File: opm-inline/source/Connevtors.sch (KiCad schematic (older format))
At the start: 23 parts

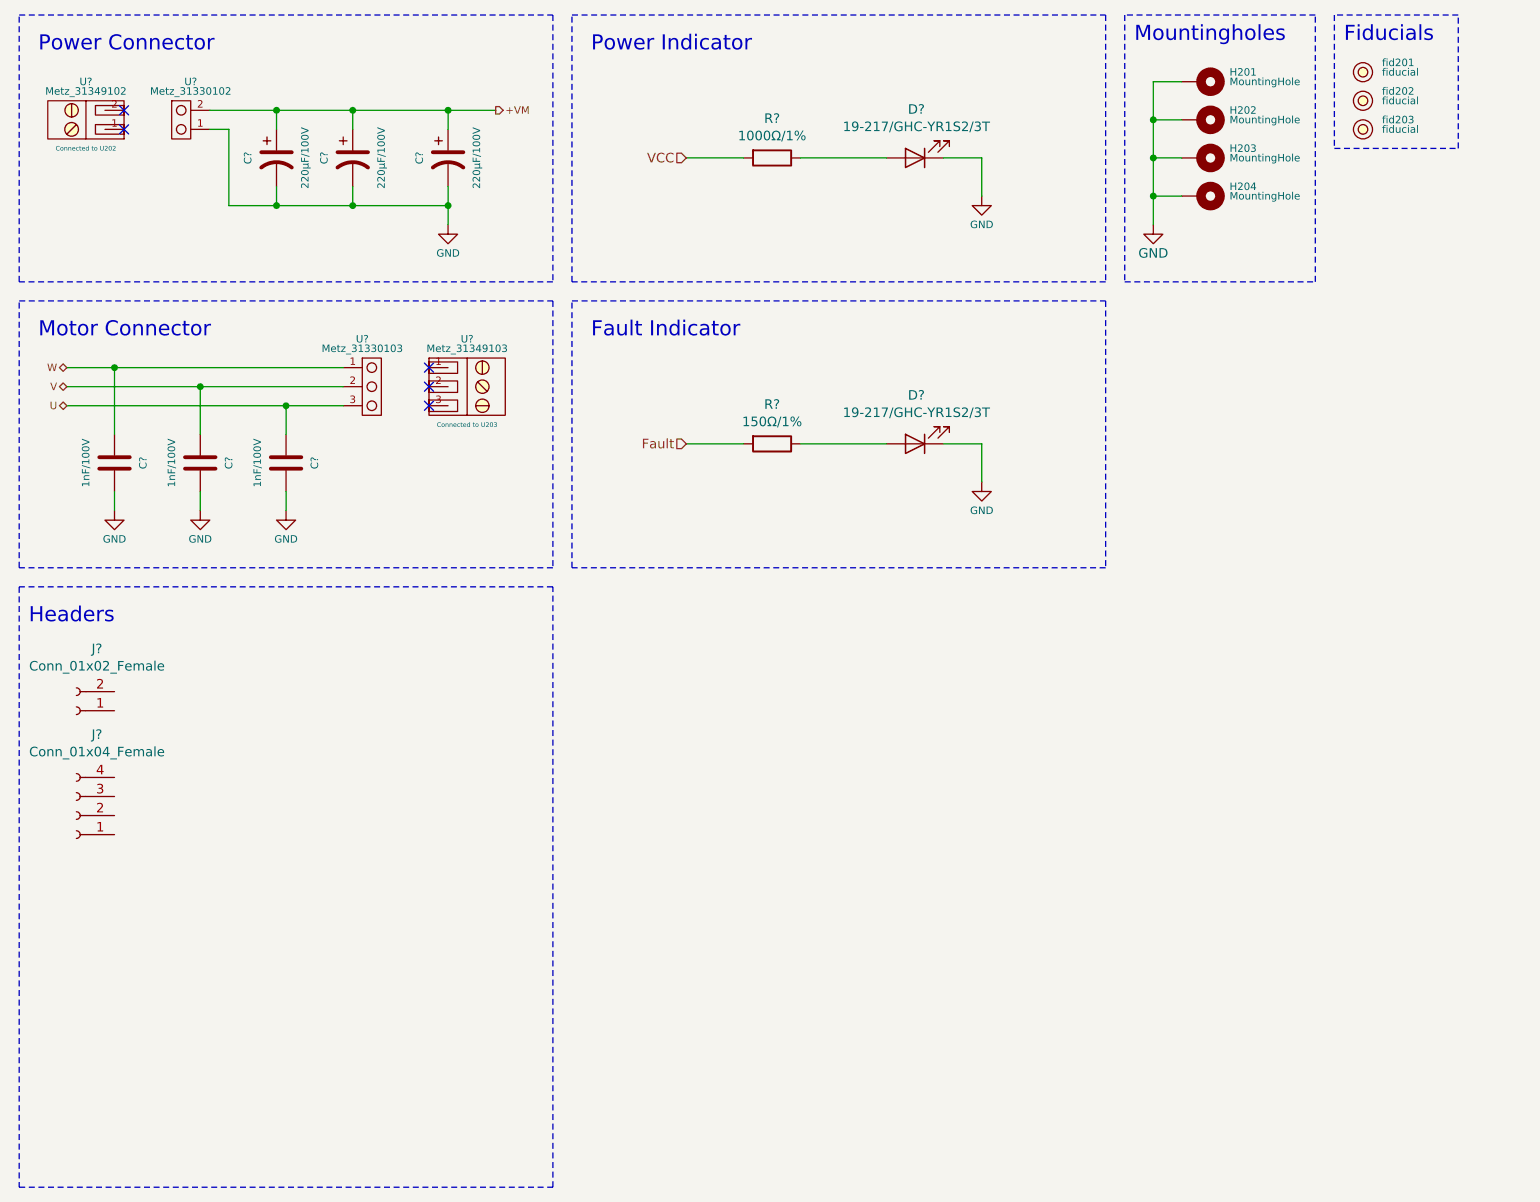
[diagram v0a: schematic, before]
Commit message: add headers
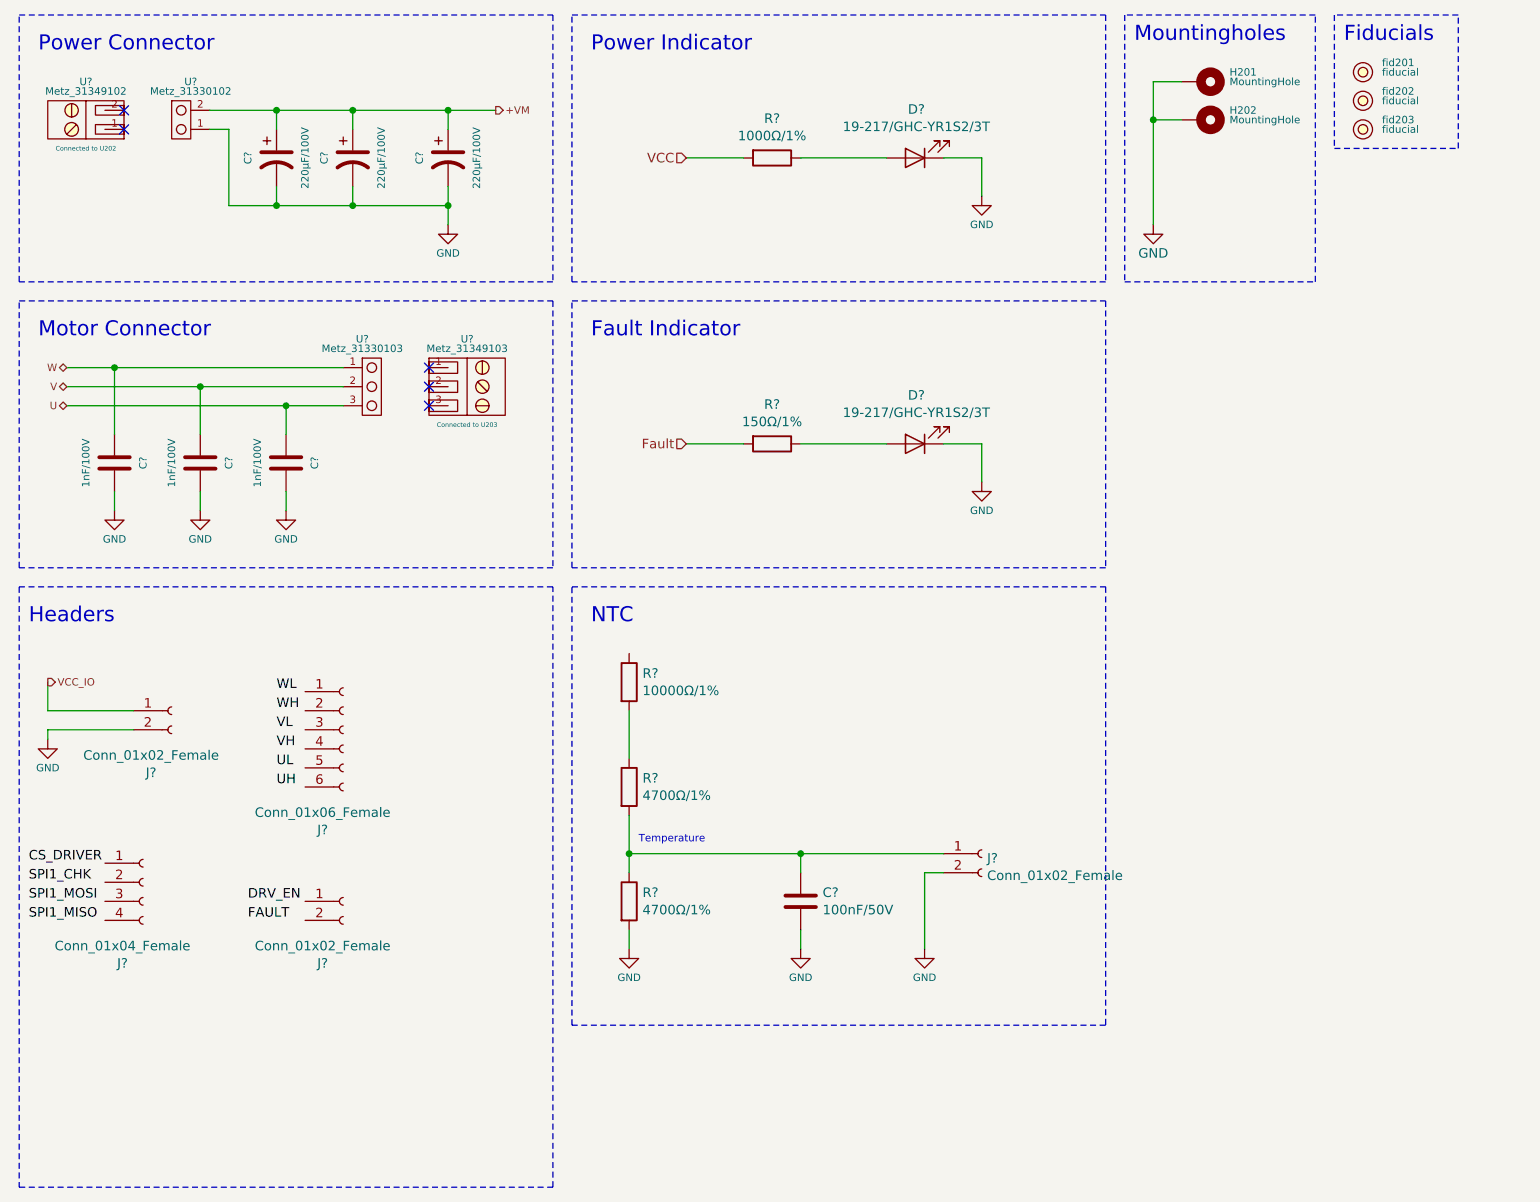
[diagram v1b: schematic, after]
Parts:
- removed H203, H204: MountingHole, MountingHole:MountingHole_3.2mm_M3_Pad, symbol opm-cache:Mechanical_MountingHole_Pad
- added C?: 100nF/50V, Capacitor_SMD:C_0603_1608Metric, symbol Device:C
- added J? (x2): Conn_01x02_Female, symbol Connector:Conn_01x02_Female
- added J?: Conn_01x06_Female, symbol Connector:Conn_01x06_Female
- added R? (x2): 4700Ω/1%, symbol Device:R
- added R?: 10000Ω/1%, Resistor_SMD:R_0603_1608Metric, symbol Device:R
- J? (x2): footprint (none) -> Connector_PinHeader_2.00mm:PinHeader_1x02_P2.00mm_Vertical
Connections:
- net GND: now also J?.2 (Pin_2), C?.2, J?.2 (Pin_2), R?.2
- net VCC_IO: now reaches J?.1 (Pin_1)
- new net: C?.1, J?.1 (Pin_1), R?.1, R?.2
- new net: R?.1, R?.2
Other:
- note added: "NTC"
- note added: "Temperature"
- moved on the sheet: J?

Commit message: prepare for pcb
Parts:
- R17, R18: renamed from R?; footprint (none) -> Resistor_SMD:R_0603_1608Metric
- fid201, fid202, fid203: footprint Fiducial:Fiducial_0.5mm_Dia_1mm_Outer -> Fiducial:Fiducial_0.5mm_Mask1mm
- gave numbers to parts that had none: 21
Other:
- moved on the sheet: J1, J2, J3, J4

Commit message: fix connections
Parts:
- added R21: 1000Ω/1%, symbol Device:R
- added R22: 0Ω, symbol Device:R
- added R23: 1500Ω/1%, symbol Device:R
- added R24: 4700Ω/1%, symbol Device:R
- C13, C15, C16: footprint Capacitor_THT:CP_Radial_D12.5mm_P5.00mm -> Libraries:CAPE830X690N
- J1: footprint Connector_PinHeader_2.00mm:PinHeader_1x02_P2.00mm_Vertical -> Connector_PinHeader_2.54mm:PinHeader_1x04_P2.54mm_Vertical
- J2: footprint Connector_PinHeader_2.00mm:PinHeader_1x02_P2.00mm_Vertical -> Connector_PinHeader_2.54mm:PinHeader_1x02_P2.54mm_Vertical
- J3: footprint (none) -> Connector_PinHeader_2.54mm:PinHeader_1x06_P2.54mm_Vertical
- J4, J5: footprint (none) -> Connector_PinHeader_2.54mm:PinHeader_1x02_P2.54mm_Vertical
- U1: footprint (none) -> TerminalBlock:TerminalBlock_bornier-2_P5.08mm
- U4: footprint (none) -> TerminalBlock:TerminalBlock_bornier-3_P5.08mm
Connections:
- net DRV_EN: now also J4.1 (Pin_1)
- net FAULT: now also J4.2 (Pin_2)
- net GND: now also R22.2, R24.2
- net SPI1_CHK: now also J1.2 (Pin_2)
- net SPI1_MISO: now also J1.3 (Pin_3), J1.4 (Pin_4)
- net UH: now also J3.6 (Pin_6)
- net UL: now also J3.5 (Pin_5)
- net VH: now also J3.4 (Pin_4)
- net VL: now also J3.3 (Pin_3)
- net WH: now also J3.2 (Pin_2)
- net WL: now also J3.1 (Pin_1)
- net ~CS_DRIVER: now reaches J1.1 (Pin_1)
- new net +VCC_IO: R21.1, R23.1
- new net SPE: R23.2, R24.1
- new net VOFS: R21.2, R22.1
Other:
- note added: "Not Mounted"
- note added: "VCC_IO SPE"
- note added: "VCC_IO VOFS"
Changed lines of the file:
@@
 F 0 "U4" V 2700 2700 39  0000 C CNN
 F 1 "Metz_31349103" V 2750 2700 39  0000 C CNN
-F 2 "" H 2925 2770 39  0001 C CNN
-F 3 "http://www.farnell.com/datasheets/2336351.pdf" H 2925 2770 39  0001 C CNN
+F 2 "TerminalBlock:TerminalBlock_bornier-3_P5.08mm" H 2925 2770 39  0001 C CNN
+F 3 "" H 2925 2770 39  0001 C CNN
 F 4 "Connected to U203" V 3150 2700 24  0000 C CNN "Info"
 	1    2950 2700
@@
 F 0 "U1" V 1150 1300 39  0000 C CNN
 F 1 "Metz_31349102" V 1100 1300 39  0000 C CNN
-F 2 "" H 950 1250 39  0001 C CNN
+F 2 "TerminalBlock:TerminalBlock_bornier-2_P5.08mm" H 950 1250 39  0001 C CNN
 F 3 "" H 950 1250 39  0001 C CNN
 F 4 "Connected to U202" V 800 1300 24  0000 C CNN "Info"
@@
 F 0 "C15" V 2200 1500 39  0000 C CNN
 F 1 "220μF/100V" V 2500 1500 39  0000 C CNN
-F 2 "Capacitor_THT:CP_Radial_D12.5mm_P5.00mm" V 2550 1500 39  0001 C CNN
+F 2 "Libraries:CAPE830X690N" V 2550 1500 39  0001 C CNN
 F 3 "~" H 2350 1500 39  0001 C CNN
 F 4 "C340711" V 2350 1500 50  0001 C CNN "LCSC"
@@
 F 0 "C16" V 2700 1500 39  0000 C CNN
 F 1 "220μF/100V" V 3000 1500 39  0000 C CNN
-F 2 "Capacitor_THT:CP_Radial_D12.5mm_P5.00mm" H 2850 1500 39  0001 C CNN
+F 2 "Libraries:CAPE830X690N" H 2850 1500 39  0001 C CNN
 F 3 "~" H 2850 1500 39  0001 C CNN
 F 4 "C340711" V 2850 1500 50  0001 C CNN "LCSC"
@@
 F 0 "C13" V 1800 1500 39  0000 C CNN
 F 1 "220μF/100V" V 2100 1500 39  0000 C CNN
-F 2 "Capacitor_THT:CP_Radial_D12.5mm_P5.00mm" V 2150 1500 39  0001 C CNN
+F 2 "Libraries:CAPE830X690N" V 2150 1500 39  0001 C CNN
 F 3 "~" H 1950 1500 39  0001 C CNN
 F 4 "C340711" V 1950 1500 50  0001 C CNN "LCSC"
@@
 F 0 "J2" H 1592 4275 50  0000 C CNN
 F 1 "Conn_01x02_Female" H 1592 4366 50  0000 C CNN
-F 2 "Connector_PinHeader_2.00mm:PinHeader_1x02_P2.00mm_Vertical" H 1700 4600 50  0001 C CNN
+F 2 "Connector_PinHeader_2.54mm:PinHeader_1x02_P2.54mm_Vertical" H 1700 4600 50  0001 C CNN
 F 3 "~" H 1700 4600 50  0001 C CNN
 	1    1700 4600
@@
 F 0 "J1" H 1442 5075 50  0000 C CNN
 F 1 "Conn_01x04_Female" H 1442 5166 50  0000 C CNN
-F 2 "Connector_PinHeader_2.00mm:PinHeader_1x02_P2.00mm_Vertical" H 1550 5500 50  0001 C CNN
+F 2 "Connector_PinHeader_2.54mm:PinHeader_1x04_P2.54mm_Vertical" H 1550 5500 50  0001 C CNN
 F 3 "~" H 1550 5500 50  0001 C CNN
 	1    1550 5500
@@
 F 0 "J5" H 5678 5126 50  0000 L CNN
 F 1 "Conn_01x02_Female" H 5678 5035 50  0000 L CNN
-F 2 "" H 5650 5150 50  0001 C CNN
+F 2 "Connector_PinHeader_2.54mm:PinHeader_1x02_P2.54mm_Vertical" H 5650 5150 50  0001 C CNN
 F 3 "~" H 5650 5150 50  0001 C CNN
 	1    5650 5150
@@
 F 0 "J3" H 2492 4175 50  0000 C CNN
 F 1 "Conn_01x06_Female" H 2492 4266 50  0000 C CNN
-F 2 "" H 2600 4700 50  0001 C CNN
+F 2 "Connector_PinHeader_2.54mm:PinHeader_1x06_P2.54mm_Vertical" H 2600 4700 50  0001 C CNN
 F 3 "~" H 2600 4700 50  0001 C CNN
 	1    2600 4700
@@
 F 0 "J4" H 2492 5275 50  0000 C CNN
 F 1 "Conn_01x02_Female" H 2492 5366 50  0000 C CNN
-F 2 "" H 2600 5600 50  0001 C CNN
+F 2 "Connector_PinHeader_2.54mm:PinHeader_1x02_P2.54mm_Vertical" H 2600 5600 50  0001 C CNN
 F 3 "~" H 2600 5600 50  0001 C CNN
 	1    2600 5600
 	1    0    0    -1
 $EndComp
-Text Label 2250 4500 0    50   ~ 0
-WL
-Text Label 2250 4800 0    50   ~ 0
-VH
-Text Label 2250 4600 0    50   ~ 0
-WH
-Text Label 2250 4700 0    50   ~ 0
-VL
-Text Label 2250 4900 0    50   ~ 0
-UL
-Text Label 2250 5000 0    50   ~ 0
-UH
-Text Label 2100 5600 0    50   ~ 0
-DRV_EN
-Text Label 2100 5700 0    50   ~ 0
-FAULT
-Text Label 950  5400 0    50   ~ 0
-CS_DRIVER
-Text Label 950  5500 0    50   ~ 0
-SPI1_CHK
-Text Label 950  5600 0    50   ~ 0
-SPI1_MOSI
-Text Label 950  5700 0    50   ~ 0
-SPI1_MISO
 Text HLabel 1050 4450 2    39   Output ~ 0
 VCC_IO
@@
 Wire Wire Line
 	1050 4700 1050 4750
+Text HLabel 1350 5700 0    50   Input ~ 0
+SPI1_MISO
+Text HLabel 2400 5000 0    50   Input ~ 0
+UH
+Text HLabel 2400 4900 0    50   Input ~ 0
+UL
+Text HLabel 2400 4800 0    50   Input ~ 0
+VH
+Text HLabel 2400 4700 0    50   Input ~ 0
+VL
+Text HLabel 2400 4600 0    50   Input ~ 0
+WH
+Text HLabel 2400 4500 0    50   Input ~ 0
+WL
+Text HLabel 2400 5600 0    50   Input ~ 0
+DRV_EN
+Text HLabel 2400 5700 0    50   Input ~ 0
+FAULT
+Text HLabel 1350 5500 0    50   Input ~ 0
+SPI1_CHK
+Text HLabel 1350 5400 0    50   Input ~ 0
+~CS_DRIVER
+Text HLabel 1350 5600 0    50   Input ~ 0
+SPI1_MISO
+$Comp
+L Device:R R21
+U 1 1 61C3D61B
+P 6850 3050
+F 0 "R21" H 6920 3096 50  0000 L CNN
+F 1 "1000Ω/1%" H 6920 3005 50  0000 L CNN
+F 2 "" V 6780 3050 50  0001 C CNN
+F 3 "~" H 6850 3050 50  0001 C CNN
+	1    6850 3050
+	1    0    0    -1
+$EndComp
+$Comp
+L Device:R R22
+U 1 1 61C3DBA6
+P 6850 3550
+F 0 "R22" H 6920 3596 50  0000 L CNN
+F 1 "0Ω" H 6920 3505 50  0000 L CNN
+F 2 "" V 6780 3550 50  0001 C CNN
+F 3 "~" H 6850 3550 50  0001 C CNN
+	1    6850 3550
+	1    0    0    -1
+$EndComp
+$Comp
+L power:GND #PWR0111
+U 1 1 61C3E273
+P 6850 3750
+F 0 "#PWR0111" H 6850 3500 39  0001 C CNN
+F 1 "GND" H 6850 3600 39  0000 C CNN
+F 2 "" H 6850 3750 50  0001 C CNN
+F 3 "" H 6850 3750 50  0001 C CNN
+	1    6850 3750
+	1    0    0    -1
+$EndComp
+Text HLabel 6850 2800 1    28   Input ~ 0
++VCC_IO
+Text HLabel 7200 3300 2    28   Input ~ 0
+VOFS
+Wire Wire Line
+	6850 3200 6850 3300
+Wire Wire Line
+	6850 2800 6850 2900
+Wire Wire Line
+	7200 3300 6850 3300
+Connection ~ 6850 3300
+Wire Wire Line
+	6850 3300 6850 3400
+Wire Wire Line
+	6850 3700 6850 3750
+Wire Notes Line
+	6400 2250 6400 4250
+Wire Notes Line
+	6400 4250 7400 4250
+Wire Notes Line
+	7400 4250 7400 2250
+Wire Notes Line
+	7400 2250 6400 2250
+Text Notes 6450 2450 0    79   ~ 0
+VCC_IO SPE
+Wire Notes Line
+	6600 3400 7200 3400
+Wire Notes Line
+	7200 3400 7200 3750
+Wire Notes Line
+	7200 3750 6600 3750
+Wire Notes Line
+	6600 3750 6600 3400
+$Comp
+L Device:R R23
+U 1 1 61C53952
+P 7950 3050
+F 0 "R23" H 8020 3096 50  0000 L CNN
+F 1 "1500Ω/1%" H 8020 3005 50  0000 L CNN
+F 2 "" V 7880 3050 50  0001 C CNN
+F 3 "~" H 7950 3050 50  0001 C CNN
+	1    7950 3050
+	1    0    0    -1
+$EndComp
+$Comp
+L Device:R R24
+U 1 1 61C53C70
+P 7950 3550
+F 0 "R24" H 8020 3596 50  0000 L CNN
+F 1 "4700Ω/1%" H 8020 3505 50  0000 L CNN
+F 2 "" V 7880 3550 50  0001 C CNN
+F 3 "~" H 7950 3550 50  0001 C CNN
+	1    7950 3550
+	1    0    0    -1
+$EndComp
+$Comp
+L power:GND #PWR0112
+U 1 1 61C53C7A
+P 7950 3750
+F 0 "#PWR0112" H 7950 3500 39  0001 C CNN
+F 1 "GND" H 7950 3600 39  0000 C CNN
+F 2 "" H 7950 3750 50  0001 C CNN
+F 3 "" H 7950 3750 50  0001 C CNN
+	1    7950 3750
+	1    0    0    -1
+$EndComp
+Text HLabel 7950 2800 1    28   Input ~ 0
++VCC_IO
+Text HLabel 8300 3300 2    28   Input ~ 0
+SPE
+Wire Wire Line
+	7950 3200 7950 3300
+Wire Wire Line
+	7950 2800 7950 2900
+Wire Wire Line
+	8300 3300 7950 3300
+Connection ~ 7950 3300
+Wire Wire Line
+	7950 3300 7950 3400
+Wire Wire Line
+	7950 3700 7950 3750
+Wire Notes Line
+	7500 2250 7500 4250
+Wire Notes Line
+	7500 4250 8500 4250
+Wire Notes Line
+	8500 4250 8500 2250
+Wire Notes Line
+	8500 2250 7500 2250
+Text Notes 7550 2450 0    79   ~ 0
+VCC_IO VOFS
+Text Notes 6900 3750 0    28   ~ 0
+Not Mounted
 $EndSCHEMATC
